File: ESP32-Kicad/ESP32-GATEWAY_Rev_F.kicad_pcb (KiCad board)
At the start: 2 copper layers, 50.8 x 62.2 mm, 64 parts, among them J1 Conn_01x07_Male, T1 DTC114YKA, U2 TLV62569DBVT(SOT23-5), U3 ESP32-WROOM-32D-4MB, U4 LAN8710A-EZC(QFN32)

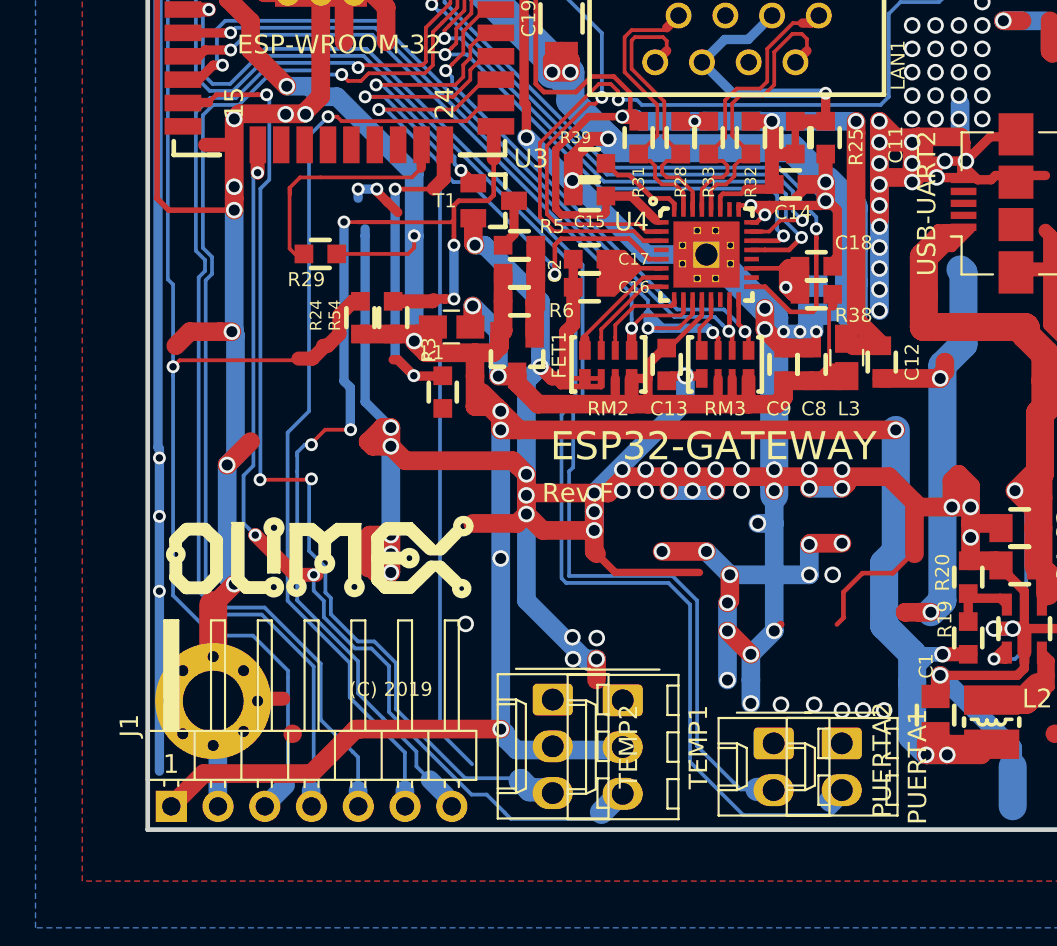
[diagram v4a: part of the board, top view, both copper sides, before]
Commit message: Proyecto en kicad actualizado
Se modificó la posición de la pinera para programar la placa. Recolocaron los conectores de los sensores y se agregaron sus resistencias mas el modelo 3D de todo esto.
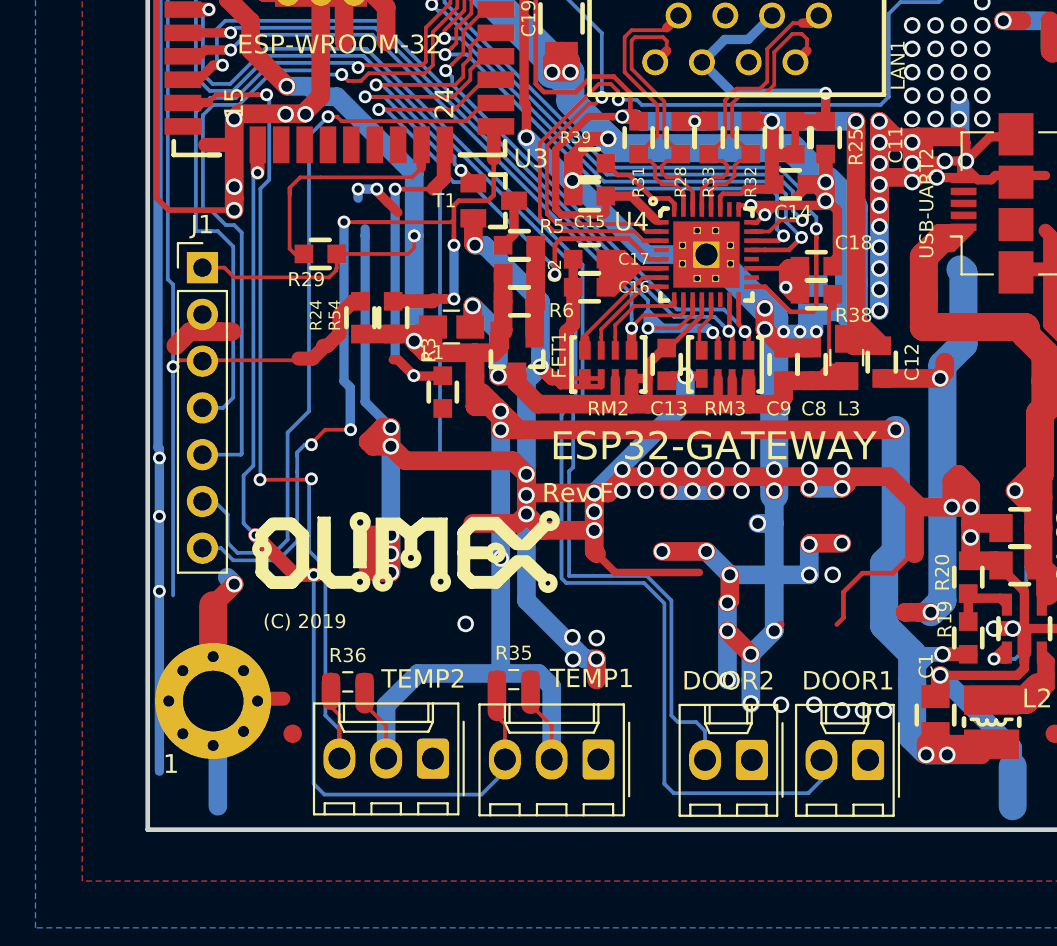
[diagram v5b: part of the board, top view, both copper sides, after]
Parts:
- removed PUERTA2: Conn_01x02_Female, Connector_Molex:Molex_KK-254_AE-6410-02A_1x02_P2.54mm_Vertical
- added DOOR2: Conn_01x02_Female, Connector_Molex:Molex_KK-254_AE-6410-02A_1x02_P2.54mm_Vertical, F.Cu at (102.4, 125.5)
- added R35: 4.7K/R0603, Resistor_SMD:R_0603_1608Metric_Pad0.98x0.95mm_HandSolder, F.Cu at (89.5, 121.1)
- added R36: 4.7K/R0603, Resistor_SMD:R_0603_1608Metric_Pad0.98x0.95mm_HandSolder, F.Cu at (80.5, 121.3)
- J1: footprint Connector_PinHeader_2.54mm:PinHeader_1x07_P2.54mm_Horizontal -> Connector_PinHeader_2.54mm:PinHeader_1x07_P2.54mm_Vertical
- moved J1 29.3 mm to (72.6, 98.8), turned to 0 degrees
- moved TEMP2 7.26 mm to (85.1, 125.4), turned to 180 degrees
- moved Logo-OlimexBIG 4.69 mm to (83.8, 114.2)
- moved TEMP1 3.48 mm to (94.1, 125.5), turned to 180 degrees
- moved DOOR1 1.70 mm to (108.7, 125.5), turned to 180 degrees
- renumbered PUERTA1 to DOOR1
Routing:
- net /GPIO1\U0TXD: track 69.1 -> 44.3 mm
- net GND: track 771.6 -> 749.6 mm, vias 190 -> 188
- net /GPIO3\U0RXD: track 66.8 -> 46.0 mm
- net /GPIO16: track 44.9 -> 27.8 mm
- net /ESP_EN: track 70.4 -> 54.6 mm
- net /GPIO0: track 59.4 -> 48.1 mm
- net /GPIO4\HS2_DATA1: track 50.6 -> 40.5 mm
- net /GPIO14\TEMP2: track 55.4 -> 49.5 mm
- net +3V3: track 168.9 -> 174.6 mm, vias 11 -> 10
- net /GPIO33\PUERTA2: track 69.3 -> 64.9 mm
- net /GPIO32\PUERTA1: track 77.9 -> 76.5 mm
- net /GPIO13\TEMP1: track 52.9 -> 53.7 mm

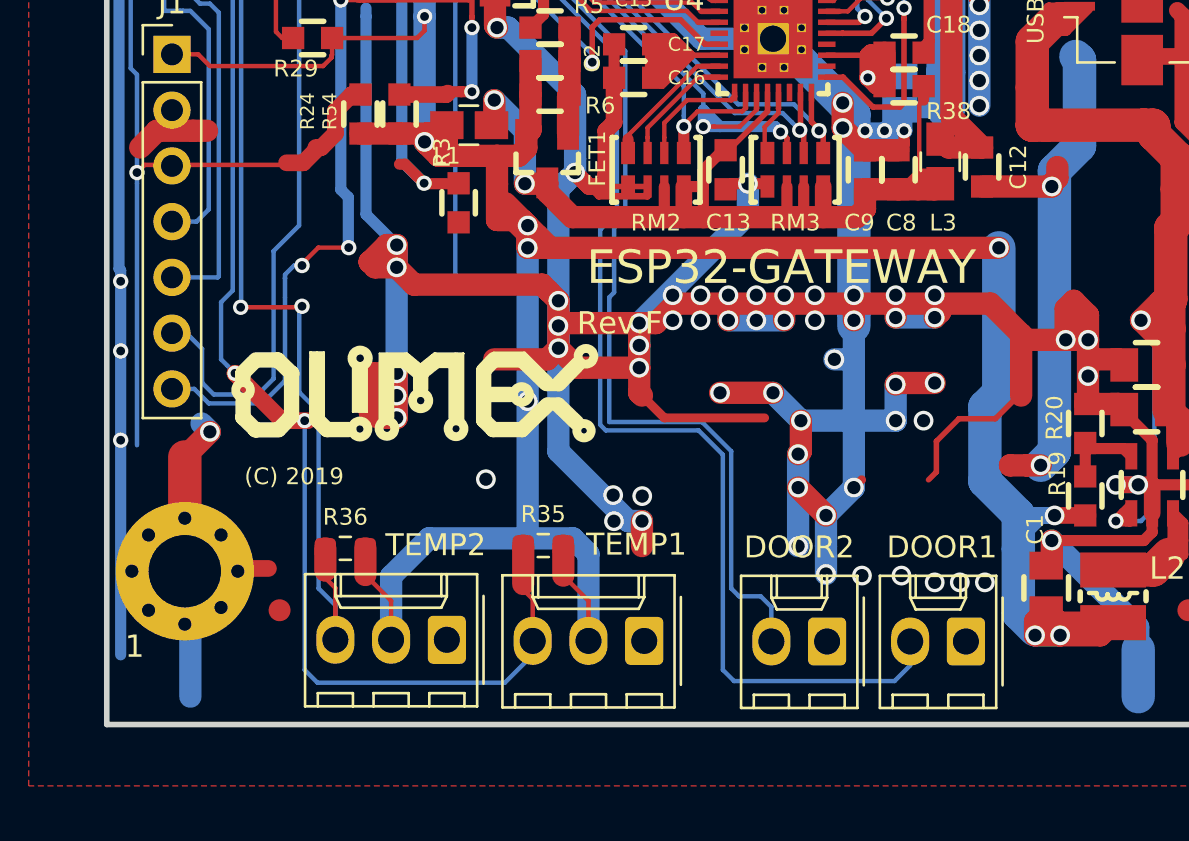
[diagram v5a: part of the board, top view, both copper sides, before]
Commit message: Proyecto en kicad actualizado
Push button agregado, se acomodaron los sensores y se agregó un capacitor a la salida de la fuente
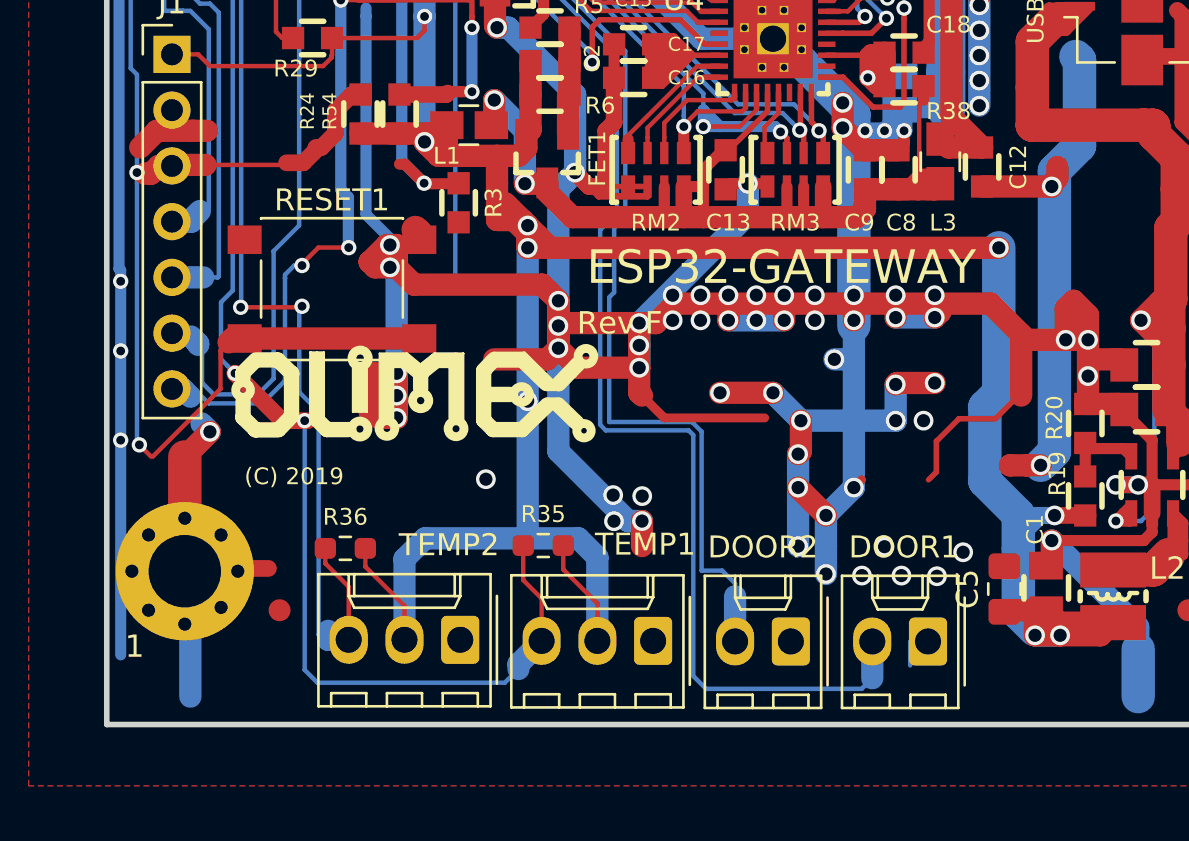
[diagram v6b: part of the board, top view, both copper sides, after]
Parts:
- added C5: 10uF/6.3V/20%/X5R/C0805/1mΩ, Capacitor_SMD:C_0805_2012Metric_Pad1.18x1.45mm_HandSolder, F.Cu at (110.5, 123.1)
- added RESET1: TAC-SWITCH SMD 6X6MM, Button_Switch_SMD:SW_SPST_PTS645, F.Cu at (79.9, 109.4)
- moved DOOR1 1.73 mm to (107.0, 125.5)
- moved DOOR2 1.65 mm to (100.8, 125.5)
- moved TEMP2 0.61 mm to (85.7, 125.4)
- moved TEMP1 0.41 mm to (94.5, 125.5)
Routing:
- net /ESP_EN: track 54.6 -> 73.9 mm, vias 2 -> 3
- net +3V3: track 174.6 -> 177.1 mm
- net /GPIO13\TEMP1: track 53.7 -> 55.6 mm
- net GND: track 749.6 -> 751.2 mm
- net /GPIO14\TEMP2: track 49.5 -> 51.1 mm
- net /GPIO1\U0TXD: track 44.3 -> 45.8 mm
- net /GPIO0: track 48.1 -> 49.0 mm
- net /GPIO33\PUERTA2: track 64.9 -> 64.0 mm
- net /GPIO4\HS2_DATA1: track 40.5 -> 41.0 mm

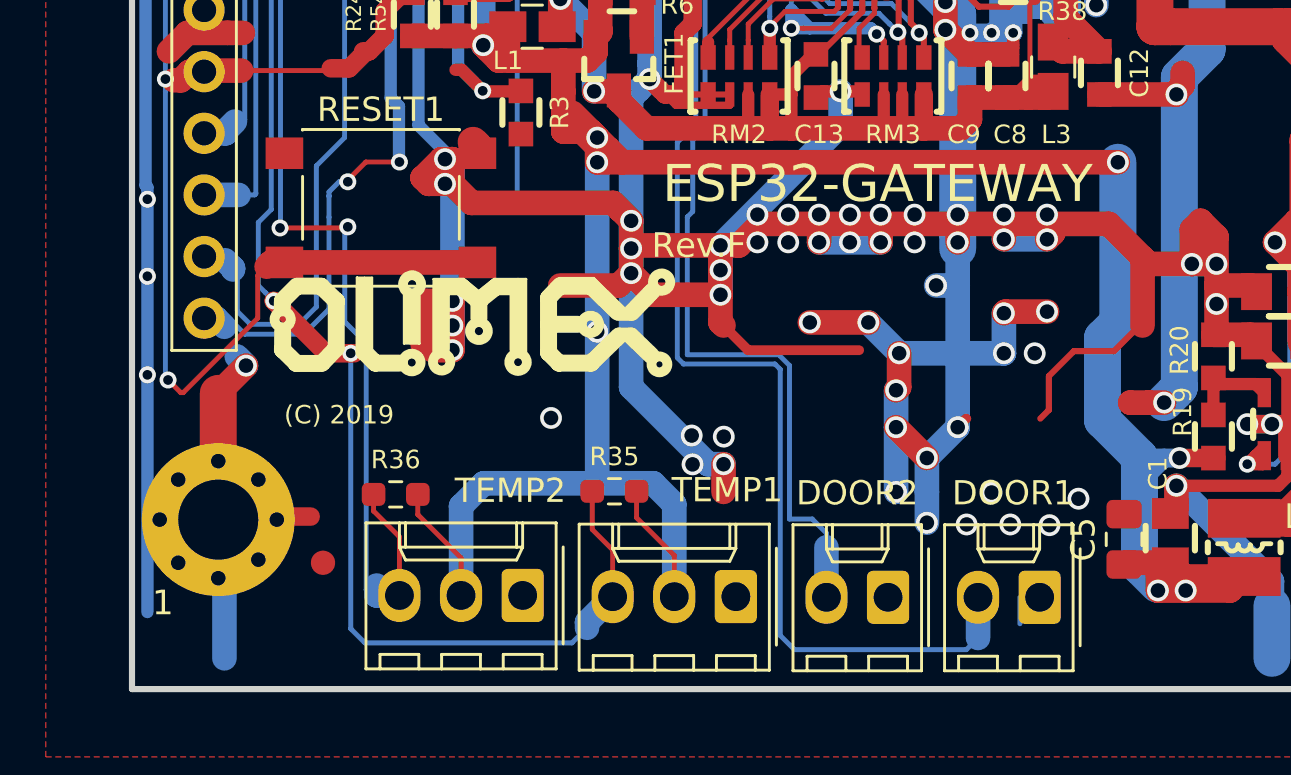
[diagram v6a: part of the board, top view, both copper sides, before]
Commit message: Proyecto en kicad actualizado
Se agregaron logos propios. Y se corrigieron otras serigrafias.
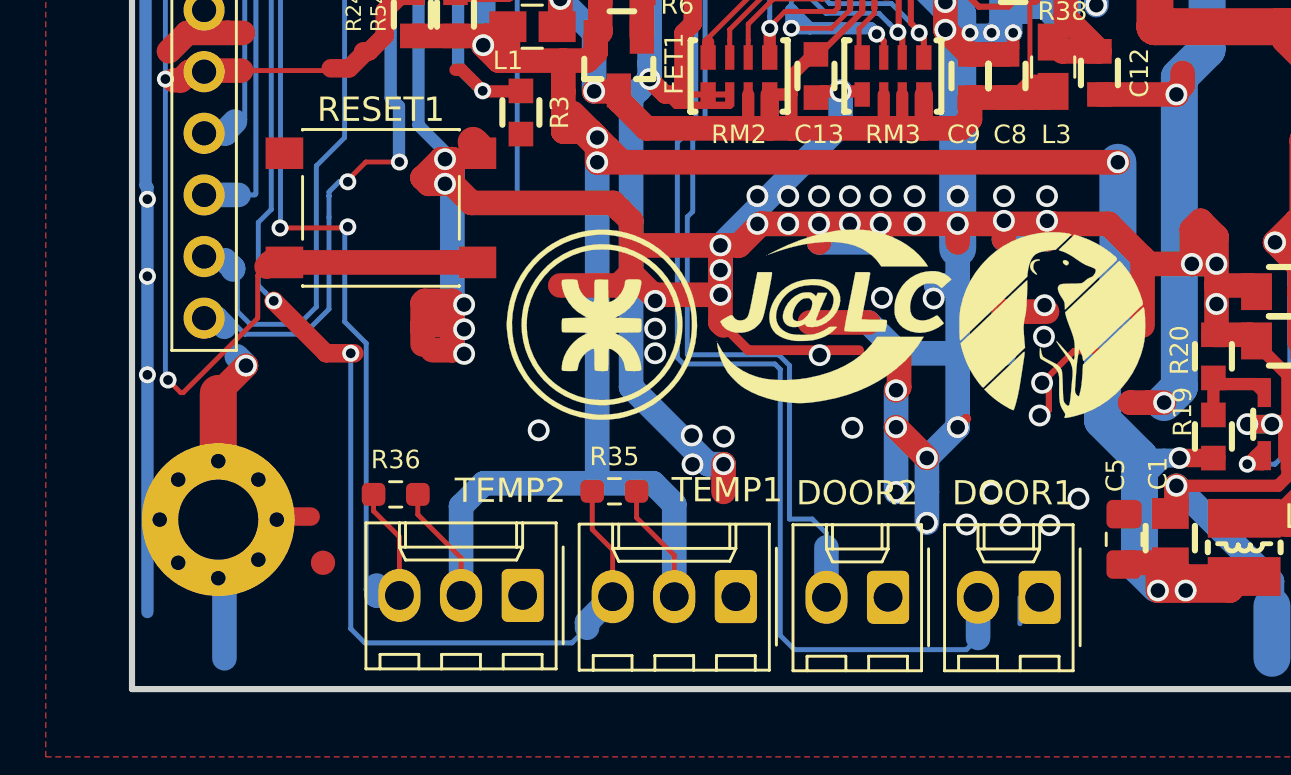
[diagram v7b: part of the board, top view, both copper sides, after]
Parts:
- removed Logo-OLimeX, Logo-OlimexBIG: , OLIMEX_LOGOs-FP:OLIMEX_LOGO_TB
- removed Logo-OSHW: , OLIMEX_LOGOs-FP:LOGO_OPENHARDWARE_8x8
- removed Sign-Antistatic: Val**, OLIMEX_LOGOs-FP:LOGO_ANTISTATIC_1
- removed Sign-RecyclBin: , OLIMEX_LOGOs-FP:LOGO_RECYCLEBIN_1
- removed Sign_Pb-Free: , OLIMEX_LOGOs-FP:LOGO_PBFREE
- removed Sign_RoHS: Val**, OLIMEX_LOGOs-FP:LOGO_ROHS_1
- added G***: LOGO, Logos personales:utn_logo, F.Cu at (88.9, 114.3)
- added G***: LOGO, Logos personales:ericnet_logo, F.Cu at (107.4, 114.6)
- added G***: LOGO, Logos personales:jlcpcb_logo, F.Cu at (98.4, 113.9)
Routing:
- net +3V3: vias 10 -> 9
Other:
- board text removed: "(C) 2019"
- board text removed: "+3.3V"
- board text removed: "+5V"
- board text removed: "1"
- board text removed: "20"
- board text removed: "ESP32-GATEWAY"
- board text removed: "ESP_EN"
- board text removed: "GND"
- board text removed: "GPI34"
- board text removed: "GPI35"
- board text removed: "GPI36"
- board text removed: "GPI39"
- board text removed: "GPIO12"
- board text removed: "GPIO13"
- board text removed: "GPIO14"
- board text removed: "GPIO15"
- board text removed: "GPIO16"
- board text removed: "GPIO17"
- board text removed: "GPIO2"
- board text removed: "GPIO32"
- board text removed: "GPIO33"
- board text removed: "GPIO4"
- board text removed: "GPIO5"
- board text removed: "PIN MAP:"
- board text removed: "Rev.F"
- board text removed: "https://www.olimex.com"

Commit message: Placa kicad actualizada
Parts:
- removed G***: LOGO, Logos personales:ericnet_logo
- removed G***: LOGO, Logos personales:jlcpcb_logo
- added R40: 440/R0603, Resistor_SMD:R_0603_1608Metric_Pad0.98x0.95mm_HandSolder, F.Cu at (103.1, 116.0)
- added R41: 440/R0603, Resistor_SMD:R_0603_1608Metric_Pad0.98x0.95mm_HandSolder, F.Cu at (96.3, 116.0)
- added U1: ACPL-217-56AE, Package_SO:SO-4_4.4x2.3mm_P1.27mm, F.Cu at (105.8, 116.5)
- added U5: ACPL-217-56AE, Package_SO:SO-4_4.4x2.3mm_P1.27mm, F.Cu at (99.0, 116.5)
- DOOR1, DOOR2: value Conn_01x02_Female -> Conn_01x02
- G1: renamed from G***; value LOGO -> Logo UTN
- TEMP1, TEMP2: value Conn_01x03_Female -> Conn_01x03
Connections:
- DOOR1 pad 2: /GPIO32\PUERTA1 -> Net-(DOOR1-Pad2)
- DOOR2 pad 2: /GPIO33\PUERTA2 -> Net-(DOOR2-Pad2)
- J1 pad 1: +3V3 -> GND
- J1 pad 2: GND -> +3V3
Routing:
- net GND: track 751.2 -> 713.7 mm, vias 188 -> 173
- net +3V3: track 177.1 -> 195.6 mm
- net /GPIO32\PUERTA1: track 76.1 -> 66.4 mm, vias 1 -> 2
- net /GPIO33\PUERTA2: track 64.0 -> 57.0 mm, vias 1 -> 2
- net Net-(DOOR1-Pad2): track 0.00 -> 6.69 mm
- net Net-(DOOR2-Pad2): track 0.00 -> 6.48 mm
- net Net-(R40-Pad1): track 0.00 -> 4.33 mm
- net Net-(R41-Pad1): track 0.00 -> 4.29 mm
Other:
- board text added: "3V3"
- board text added: "EN"
- board text added: "GND"
- board text added: "GPIO0"
- board text added: "GPIO4"
- board text added: "RX"
- board text added: "TX"
